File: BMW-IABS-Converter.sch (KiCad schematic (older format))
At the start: 57 parts, among them J1 SWD, J2 HCCPHPE24BKA90F, J3 GPIO_A0, J4 GPIO_A1, J5 GPIO_F0, J6 GPIO_F1, J7 GPIO_A2, J8 GND, Q1 IRLML0030TRPbF, Q2 IRLML0030TRPbF, Q4 IRFR9024, Q6 IRFR9024, U1 SN65HVD230, U2 STM32F042F4P6, U3 MC34063AD, U4 LM2904

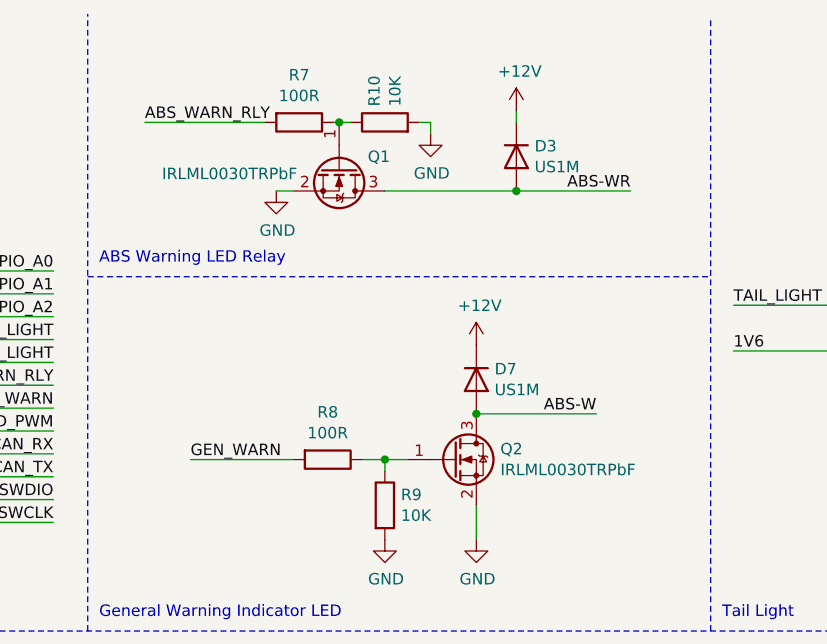
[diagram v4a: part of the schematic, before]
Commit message: Changed MOSFETS to 0030
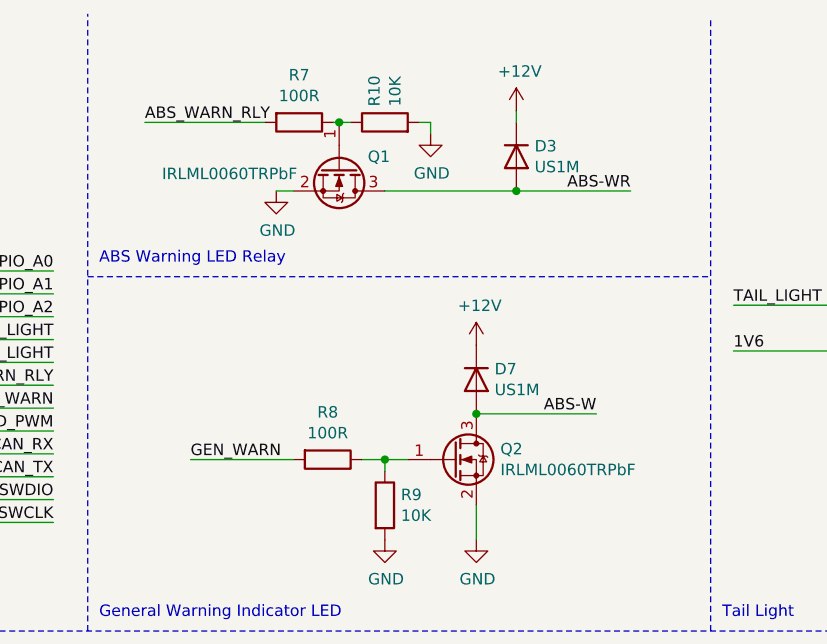
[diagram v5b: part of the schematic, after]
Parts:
- Q1, Q2: value IRLML0030TRPbF -> IRLML0060TRPbF
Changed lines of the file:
@@
 P 4900 1125
 F 0 "Q1" V 4850 1250 50  0000 L CNN
-F 1 "IRLML0030TRPbF" V 4925 350 50  0000 L CNN
+F 1 "IRLML0060TRPbF" V 4925 350 50  0000 L CNN
 F 2 "Package_TO_SOT_SMD:SOT-23" H 5100 1225 50  0001 C CNN
 F 3 "~" H 4900 1125 50  0001 C CNN
@@
 P 5400 2400
 F 0 "Q2" H 5605 2446 50  0000 L CNN
-F 1 "IRLML0030TRPbF" H 5605 2355 50  0000 L CNN
+F 1 "IRLML0060TRPbF" H 5605 2355 50  0000 L CNN
 F 2 "Package_TO_SOT_SMD:SOT-23" H 5600 2500 50  0001 C CNN
 F 3 "~" H 5400 2400 50  0001 C CNN

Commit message: Initial commit
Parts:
- added C?: 47uF 25V, symbol Device:C
- added R?: 10K, symbol Device:R
- added R?: 2K, symbol Device:R
- added R? (x2): 56K, symbol Device:R
- added R?: 100R, symbol Device:R
- added U? (x3): LMC65, symbol Device:Opamp_Dual_Generic
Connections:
- net labels added: +5V
- wire segments 154 -> 168
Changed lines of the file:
@@
 Wire Wire Line
 	7600 6125 7600 6150
+$Comp
+L Device:Opamp_Dual_Generic U?
+U 1 1 604387FE
+P 5825 4150
+F 0 "U?" H 5925 4275 50  0000 C CNN
+F 1 "LMC65" H 5800 4150 50  0000 C CNN
+F 2 "" H 5825 4150 50  0001 C CNN
+F 3 "~" H 5825 4150 50  0001 C CNN
+	1    5825 4150
+	1    0    0    -1
+$EndComp
+$Comp
+L Device:Opamp_Dual_Generic U?
+U 2 1 60438804
+P 4525 4425
+F 0 "U?" H 4525 4792 50  0000 C CNN
+F 1 "LMC65" H 4525 4701 50  0000 C CNN
+F 2 "" H 4525 4425 50  0001 C CNN
+F 3 "~" H 4525 4425 50  0001 C CNN
+	2    4525 4425
+	1    0    0    -1
+$EndComp
+$Comp
+L Device:Opamp_Dual_Generic U?
+U 3 1 6043880A
+P 5525 4175
+F 0 "U?" H 5483 4221 50  0000 L CNN
+F 1 "LMC65" H 5483 4130 50  0000 L CNN
+F 2 "" H 5525 4175 50  0001 C CNN
+F 3 "~" H 5525 4175 50  0001 C CNN
+	3    5525 4175
+	1    0    0    -1
+$EndComp
+$Comp
+L Device:R R?
+U 1 1 60438810
+P 7325 3850
+F 0 "R?" V 7118 3850 50  0000 C CNN
+F 1 "10K" V 7209 3850 50  0000 C CNN
+F 2 "" V 7255 3850 50  0001 C CNN
+F 3 "~" H 7325 3850 50  0001 C CNN
+	1    7325 3850
+	0    1    1    0
+$EndComp
+$Comp
+L Device:R R?
+U 1 1 60438816
+P 7700 4000
+F 0 "R?" H 7770 4046 50  0000 L CNN
+F 1 "2K" H 7770 3955 50  0000 L CNN
+F 2 "" V 7630 4000 50  0001 C CNN
+F 3 "~" H 7700 4000 50  0001 C CNN
+	1    7700 4000
+	1    0    0    -1
+$EndComp
+$Comp
+L Device:R R?
+U 1 1 6043881C
+P 6500 4000
+F 0 "R?" H 6430 3954 50  0000 R CNN
+F 1 "56K" H 6430 4045 50  0000 R CNN
+F 2 "" V 6430 4000 50  0001 C CNN
+F 3 "~" H 6500 4000 50  0001 C CNN
+	1    6500 4000
+	-1   0    0    -1
+$EndComp
+$Comp
+L power:+5V #PWR?
+U 1 1 60438822
+P 5425 3875
+F 0 "#PWR?" H 5425 3725 50  0001 C CNN
+F 1 "+5V" H 5440 4048 50  0000 C CNN
+F 2 "" H 5425 3875 50  0001 C CNN
+F 3 "" H 5425 3875 50  0001 C CNN
+	1    5425 3875
+	1    0    0    -1
+$EndComp
+$Comp
+L power:GND #PWR?
+U 1 1 60438828
+P 5425 4475
+F 0 "#PWR?" H 5425 4225 50  0001 C CNN
+F 1 "GND" H 5430 4302 50  0000 C CNN
+F 2 "" H 5425 4475 50  0001 C CNN
+F 3 "" H 5425 4475 50  0001 C CNN
+	1    5425 4475
+	1    0    0    -1
+$EndComp
+$Comp
+L Device:R R?
+U 1 1 6043882E
+P 4500 3925
+F 0 "R?" V 4293 3925 50  0000 C CNN
+F 1 "56K" V 4384 3925 50  0000 C CNN
+F 2 "" V 4430 3925 50  0001 C CNN
+F 3 "~" H 4500 3925 50  0001 C CNN
+	1    4500 3925
+	0    1    1    0
+$EndComp
+Wire Wire Line
+	4350 3925 4225 3925
+Wire Wire Line
+	4225 3925 4225 4325
+Wire Wire Line
+	4825 4425 4825 3925
+Wire Wire Line
+	4825 3925 4650 3925
+Text Label 8100 4150 2    50   ~ 0
+TAS
+Text Label 8100 3850 2    50   ~ 0
+TA-
+Wire Wire Line
+	8100 4150 7700 4150
+Wire Wire Line
+	7700 3850 8100 3850
+Wire Wire Line
+	7700 3850 7475 3850
+Connection ~ 7700 3850
+$Comp
+L Device:C C?
+U 1 1 6043883E
+P 7325 4150
+F 0 "C?" V 7577 4150 50  0000 C CNN
+F 1 "47uF 25V" V 7486 4150 50  0000 C CNN
+F 2 "" H 7363 4000 50  0001 C CNN
+F 3 "~" H 7325 4150 50  0001 C CNN
+	1    7325 4150
+	0    1    1    0
+$EndComp
+Connection ~ 7700 4150
+Wire Wire Line
+	7700 4150 7475 4150
+Wire Wire Line
+	6825 4150 6500 4150
+Wire Wire Line
+	6125 4150 6500 4150
+Connection ~ 6500 4150
+Wire Wire Line
+	6500 3850 5525 3850
+Wire Wire Line
+	5525 3850 5525 4050
+Connection ~ 6500 3850
+$Comp
+L Device:R R?
+U 1 1 6043884C
+P 6975 4150
+F 0 "R?" V 6768 4150 50  0000 C CNN
+F 1 "100R" V 6859 4150 50  0000 C CNN
+F 2 "" V 6905 4150 50  0001 C CNN
+F 3 "~" H 6975 4150 50  0001 C CNN
+	1    6975 4150
+	0    1    1    0
+$EndComp
+Wire Wire Line
+	7175 4150 7125 4150
+Wire Wire Line
+	6500 3850 7175 3850
 $EndSCHEMATC

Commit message: Updated schematic
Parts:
- removed R? (x2): 56K, symbol Device:R
- removed U?: LMC65, symbol Device:Opamp_Dual_Generic
- added C? (x2): C, symbol Device:C
- added R? (x2): 10K, symbol Device:R
- added R? (x2): 20K, symbol Device:R
- added R?: 15K, symbol Device:R
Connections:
- wire segments 168 -> 177
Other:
- note added: "Signal center point (GND)"
- note added: "Signal to speedometer"
- moved on the sheet: C?, R?

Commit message: Updated schematic and layout
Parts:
- removed C10: 330uF (EZV331M0JRC8), Capacitor_SMD:CP_Elec_6.3x7.7, symbol Device:CP
- removed C? (x2): C, symbol Device:C
- removed C?: 47uF 25V, symbol Device:C
- removed NT2: TA- Tie, NetTie:NetTie-2_SMD_Pad0.5mm, symbol Device:Net-Tie_2
- removed R17: 1K, Resistor_SMD:R_0402_1005Metric, symbol Device:R
- removed R? (x3): 10K, symbol Device:R
- removed R? (x2): 20K, symbol Device:R
- removed R?: 2K, symbol Device:R
- removed R?: 100R, symbol Device:R
- removed R?: 15K, symbol Device:R
- removed U? (x2): LMC65, symbol Device:Opamp_Dual_Generic
- added C10, C15: 4.7uF, Capacitor_SMD:C_0805_2012Metric, symbol Device:C
- added C6: 10uF, Capacitor_SMD:C_0805_2012Metric, symbol Device:C
- added C8: 47uF 25V, Capacitor_THT:C_Radial_D6.3mm_H11.0mm_P2.50mm, symbol Device:C
- added C9: 100nF, Capacitor_SMD:C_0402_1005Metric, symbol Device:C
- added R10, R8: 20K, Resistor_SMD:R_0603_1608Metric, symbol Device:R
- added R11: 2K, Resistor_SMD:R_1206_3216Metric, symbol Device:R
- added R12: 100R, Resistor_SMD:R_0402_1005Metric, symbol Device:R
- added R14: 10K, Resistor_SMD:R_0402_1005Metric, symbol Device:R
- added R15: 10K 1%, Resistor_SMD:R_0402_1005Metric, symbol Device:R
- added R16: 10K 1% (NC), Resistor_SMD:R_0402_1005Metric, symbol Device:R
- added R9: 10K, Resistor_SMD:R_1206_3216Metric, symbol Device:R
- added U3: LMC662AIM, Package_SO:SOIC-8_3.9x4.9mm_P1.27mm, symbol eec:LMC662AIM
- added U5: AMS1117-3.3, Package_TO_SOT_SMD:SOT-223-3_TabPin2, symbol Regulator_Linear:AMS1117-3.3
- C11: value 1uF -> 4.7uF
- C12: renamed from C2; value 220uF (EZV221M16RC8) -> 10uF; footprint Capacitor_SMD:CP_Elec_6.3x7.7 -> Capacitor_SMD:C_1206_3216Metric
- C13: renamed from C9; value 330uF (EZV331M0JRC8) -> 220uF (TAJD227K006RNJ-AVX); footprint Capacitor_SMD:CP_Elec_6.3x7.7 -> Capacitor_Tantalum_SMD:CP_EIA-7343-31_Kemet-D
- R19: renamed from R6; value 3.3K 1% -> 3K 1%
- R20: renamed from R11; footprint Resistor_SMD:R_0603_1608Metric -> Resistor_SMD:R_0805_2012Metric
- R21: renamed from R5; value 2K 1% -> 1K 1%
- R22: renamed from R12; footprint Resistor_SMD:R_0603_1608Metric -> Resistor_SMD:R_0805_2012Metric
- renumbered C6 to C14, C3 to C2, C5 to C3, C7 to C4, C8 to C5, C4 to C7, D7 to D1, D3 to D2, D4 to D3, D6 to D4, D1 to D6, D2 to D7, LOGO2 to LOGO1, LOGO1 to LOGO2, Q4 to Q1, Q1 to Q3, Q6 to Q4, R13 to R1, R3 to R13, R1 to R17, R4 to R18, R8 to R3, R7 to R4, R10 to R5, R9 to R6, R14 to R7, U4 to U1, U1 to U4, U3 to U6
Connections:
- net labels removed: +3V3
- wire segments 177 -> 166
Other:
- note added: "Vin=12v Vout=5v Iout=750mA\nFmin = 86kHz Vripl=10mV"
- note removed: "Signal center point (GND)"
- note removed: "Signal to speedometer"
- note removed: "Speedometer Output"
- note removed: "Vin=12v Vout=3.3v Iout=750mA\nFmin = 86kHz Vripl=10mV"
- moved on the sheet: C12, D1, D2, D3, Q1, Q2, Q3, R1, R20, R22, R3, R4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
